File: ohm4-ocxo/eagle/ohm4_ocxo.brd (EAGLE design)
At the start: 34 x 43.2 mm, 17 parts, among them U1 TPS73650, U2 TLV1117, X1 BU-SMA-V, X2 U.FL

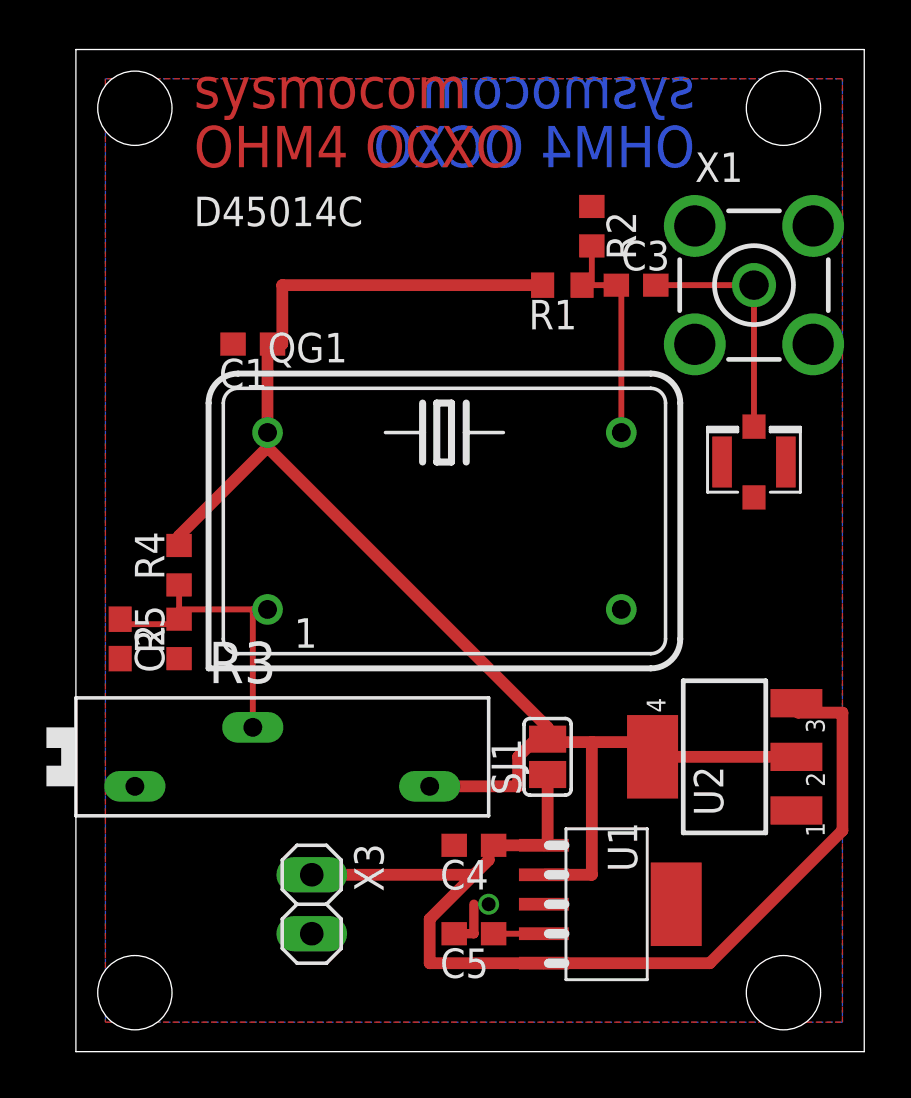
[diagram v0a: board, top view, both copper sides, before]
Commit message: update to version with PLL ic onboard
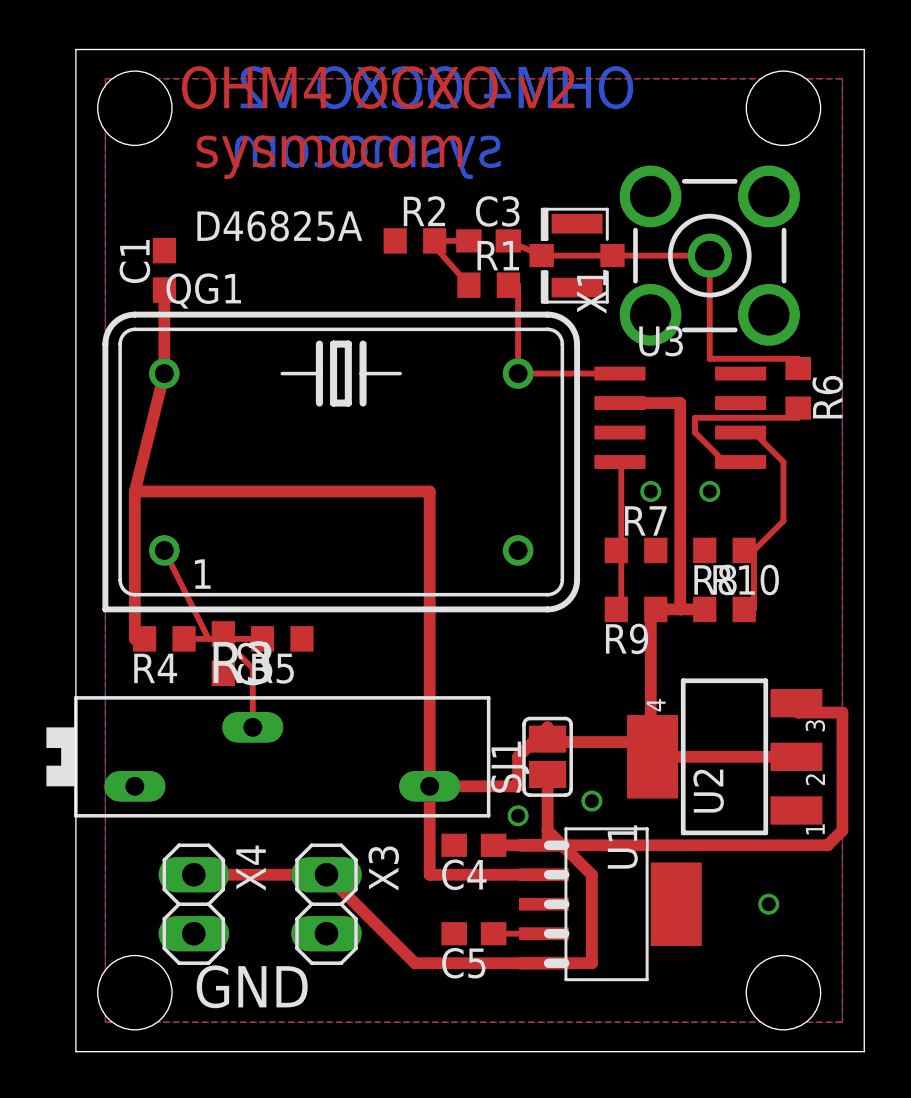
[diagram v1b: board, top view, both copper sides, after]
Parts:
- added R10, R7, R8, R9: NC, rcl:R0603
- added R6: 33, rcl:R0603
- added U3: IDT_ICS501, laforge:SOIC08
- added X4: (no value), pinhead:1X02
- C1, C2, C5: value (none) -> 10nF
- C4: value (none) -> 1uF
- moved X2 11.7 mm to (21.6, 34.3), turned to 180 degrees
- moved R2 7.65 mm to (14.6, 34.9), turned to 0 degrees
- moved C3 6.63 mm to (17.8, 34.9)
- moved QG1 5.12 mm to (11.4, 25.4)
- moved C1 4.96 mm to (3.81, 33.7), turned to 90 degrees
- moved C2 4.49 mm to (6.35, 17.1)
- moved R5 4.45 mm to (8.89, 17.8), turned to 180 degrees
- moved R4 3.24 mm to (3.81, 17.8), turned to 180 degrees
- moved R1 3.17 mm to (17.8, 33.0), turned to 0 degrees
- moved X1 2.29 mm to (27.3, 34.3), turned to 90 degrees
- moved X3 0.63 mm to (10.8, 6.35)
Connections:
- new net N$6: QG1.8, R1.2, U3.1
- new net N$7: R6.2, U3.5
- new net N$8: R7.1, R9.2, U3.4
- new net N$9: R10.2, R8.1, U3.6
- net 5V: now also R10.1, R9.1, U3.2; no longer R1.2
- net GND: now also R7.2, R8.2, U3.3, X4.2
- net N$1: no longer QG1.8
- net N$3: now also X4.1
- net N$4: now also R6.1
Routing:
- net 5V: track 68.4 -> 89.0 mm
- net N$9: track 0.00 -> 10.1 mm
- net N$6: track 0.00 -> 8.62 mm
- net N$7: track 0.00 -> 7.99 mm
- net N$4: track 10.3 -> 17.5 mm
- net N$8: track 0.00 -> 6.84 mm
- net N$1: track 9.73 -> 4.24 mm
- net N$3: track 46.3 -> 51.1 mm
- net GND: track 2.12 -> 0.00 mm, vias 1 -> 5
- net N$5: track 13.3 -> 12.2 mm
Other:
- board text added: "D46825A"
- board text added: "GND"
- board text added: "OHM4 OCXO v2"
- board text removed: "D45014C"
- board text removed: "OHM4 OCXO"

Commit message: update OHM4 OCXO, preliminary v3
 * use new LDO (single LDO with range up to 12V input)
 * add U.FL clock input (instead of OCXO as source)
 * no parallel, but series resistors to trimmer
 * allow output of PLL to be fed through resistive divider
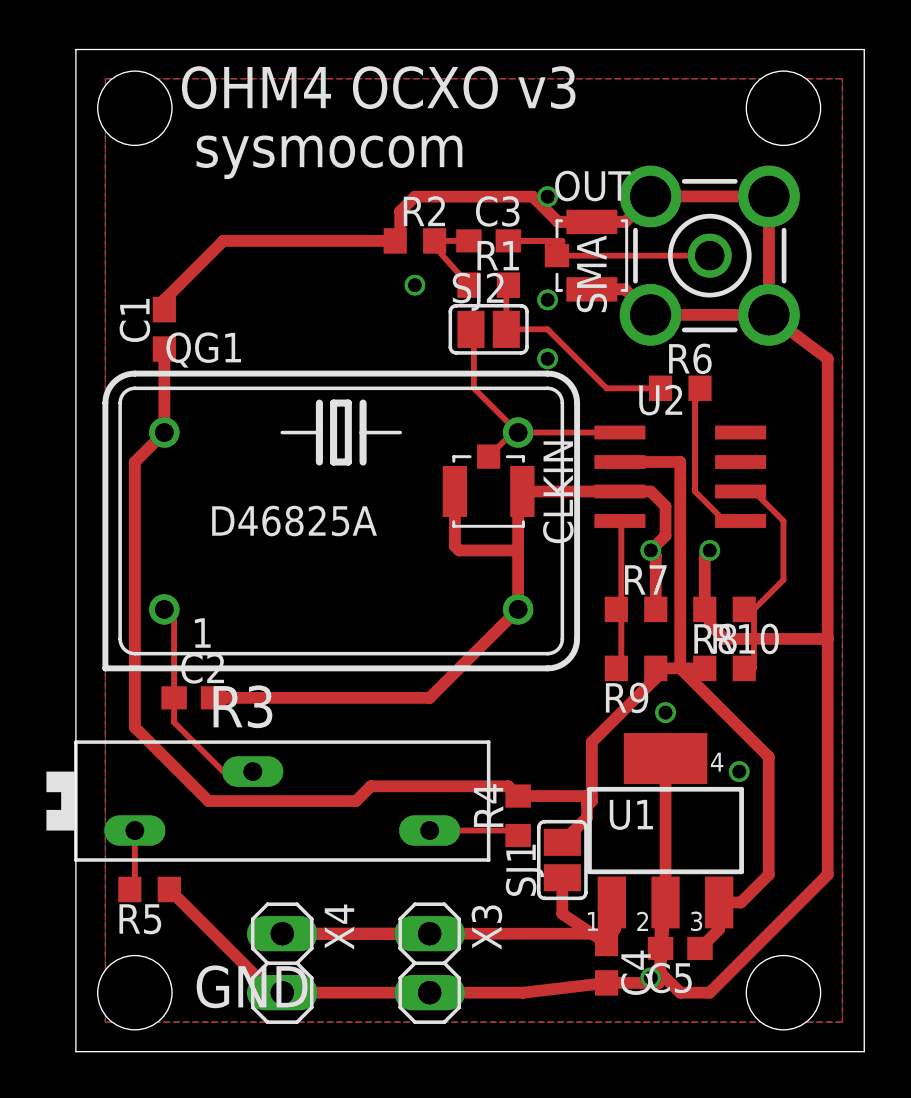
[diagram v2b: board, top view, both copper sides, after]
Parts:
- removed U3: IDT_ICS501, laforge:SOIC08
- removed X2: U.FL, SparkFun-Connectors:U.FL
- added CLKIN, OUT: (no value), laforge:HRS_UFL
- added SJ2: (no value), jumper:SJ
- C5: value 10nF -> 220nF
- R3: value (none) -> 100
- R4: value (none) -> 649
- R5: value (none) -> 365
- U1: value TPS73650 -> MC33275ST; device laforge:SOT223-6 -> laforge:SOT223
- U2: value TLV1117 -> IDT_ICS501; device laforge:SOT223 -> laforge:SOIC08
- moved R4 17.0 mm to (19.1, 10.2), turned to 90 degrees
- moved R5 12.2 mm to (3.17, 6.99)
- moved U2 12.2 mm to (26.0, 24.8), turned to 270 degrees
- moved C5 8.91 mm to (26.0, 4.45)
- moved C4 7.65 mm to (22.9, 3.81), turned to 270 degrees
- moved X3 5.12 mm to (15.2, 3.81)
- moved R6 5.08 mm to (26.0, 28.6), turned to 0 degrees
- moved X4 4.58 mm to (8.89, 3.81)
- moved SJ1 4.49 mm to (21.0, 8.26)
- moved U1 4.07 mm to (25.4, 9.53), turned to 0 degrees
- moved C1 2.54 mm to (3.81, 31.1)
- moved QG1 2.54 mm to (11.4, 22.9)
- moved R10 2.54 mm to (27.9, 16.5)
- moved R7 2.54 mm to (24.1, 19.1)
- moved R8 2.54 mm to (27.9, 19.1)
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- renumbered X1 to SMA
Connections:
- removed net 5V: C1.1, QG1.14, R10.1, R3.E, R4.2, R9.1, SJ1.2, U1.2, U2.2, U2.4, U3.2
- removed net N$2: C5.1, U1.4
- new net N$10: R3.A, R5.2
- new net N$11: R3.E, R4.1
- new net N$12: C3.2, OUT.SIG, SMA.1
- new net U1: C1.1, C5.1, QG1.14, R10.1, R4.2, R9.1, SJ1.2, U1.3, U2.2
- net GND: now also CLKIN.GND@1, CLKIN.GND@2, OUT.GND@1, OUT.GND@2, U1.2, U1.4, U2.3; no longer R3.A, U1.3, U1.6, U2.1, U3.3, X2.P$1, X2.P$2
- net N$3: no longer U1.5, U2.3
- net N$4: now also R1.2, SJ2.2; no longer C3.2, SMA.1, X2.P$3
- net N$5: no longer R4.1, R5.2
- net N$6: now also CLKIN.SIG, SJ2.1, U2.1; no longer R1.2, U3.1
- net N$7: now also U2.5; no longer U3.5
- net N$8: now also U2.4; no longer U3.4
- net N$9: now also U2.6; no longer U3.6
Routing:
- net GND: track 0.00 -> 158.6 mm, vias 5 -> 9
- net 5V: track 89.0 -> 0.00 mm
- net U1: track 0.00 -> 77.0 mm
- net N$3: track 51.1 -> 26.7 mm
- net N$12: track 0.00 -> 12.0 mm
- net N$4: track 17.5 -> 9.64 mm
- net N$11: track 0.00 -> 3.90 mm
- net N$5: track 12.2 -> 9.31 mm
- net N$6: track 8.62 -> 11.3 mm
- net N$10: track 0.00 -> 2.63 mm
- net N$2: track 2.16 -> 0.00 mm
- net N$7: track 7.99 -> 6.97 mm
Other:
- board text added: "OHM4 OCXO v3"

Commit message: final v3 as it goes in pcb production
* smash components and move labels to where they can be read
* add indication of + / GND to X3/X4
* re-route some traces to ensure sufficient distance between them
* make all traces 0.508 mm wide, even signal traces.
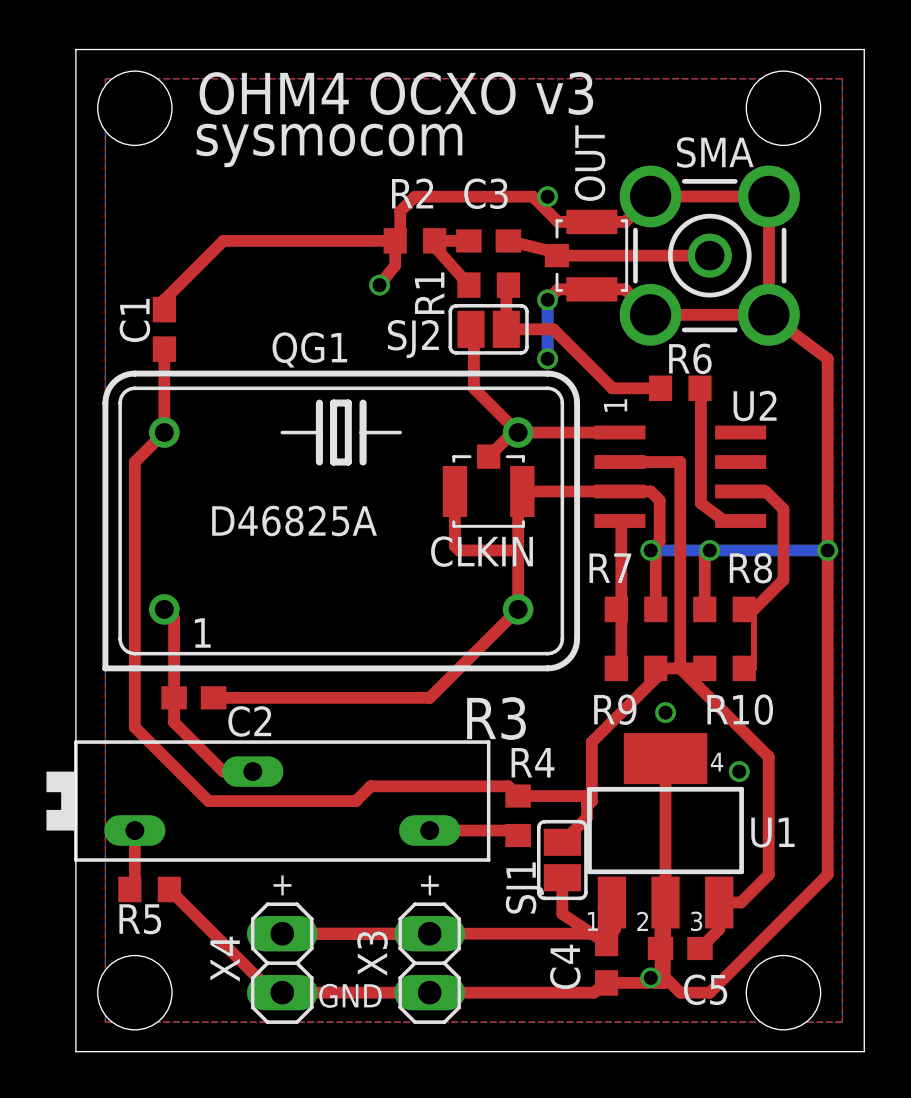
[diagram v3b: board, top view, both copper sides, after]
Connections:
- net U1 renamed VCC
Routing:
- net GND: track 158.6 -> 167.2 mm, vias 9 -> 10
- net N$12: track 12.0 -> 11.0 mm
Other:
- board text added: "+"
- board text added: "1"
- board text removed: "OHM4 OCXO v2"
